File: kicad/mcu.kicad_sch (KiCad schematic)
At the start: 40 parts, among them J1 USB_C_Receptacle_USB2.0_16P, J2 2x5x1.27mm, U4 STM32F103CBT6, U5 USBLC6-2SC6, Y1 16MHz

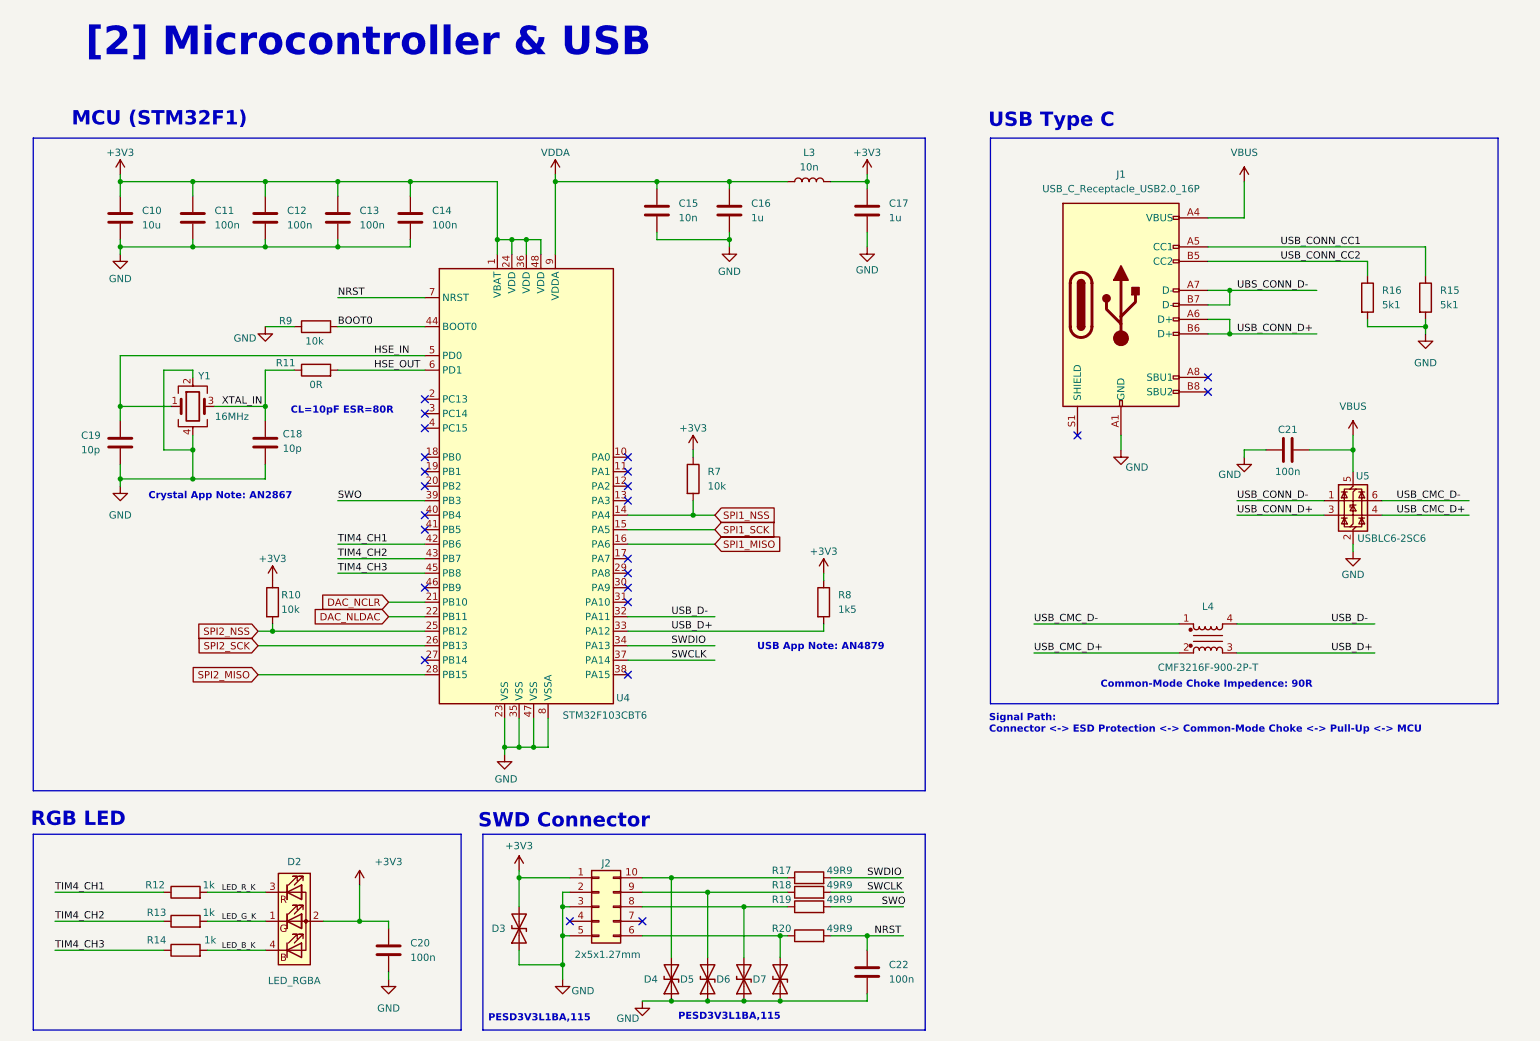
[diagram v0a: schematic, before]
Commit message: Updated parts numbering and notes
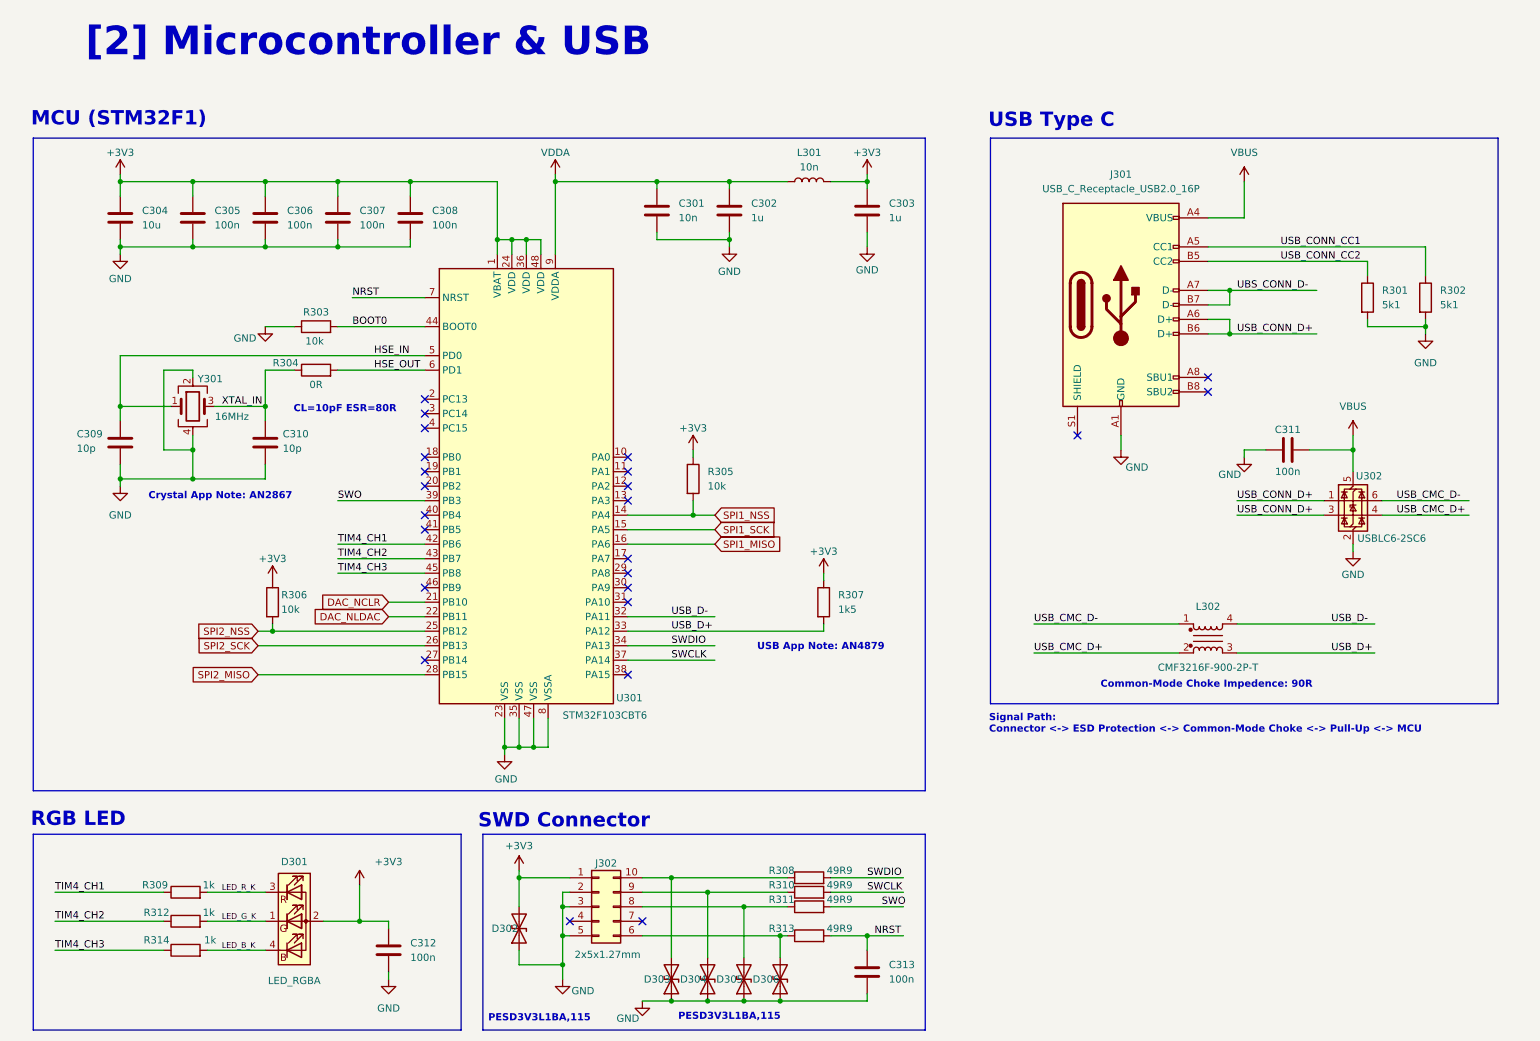
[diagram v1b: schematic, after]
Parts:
- renumbered C15 to C301, C16 to C302, C17 to C303, C10 to C304, C11 to C305, C12 to C306, C13 to C307, C14 to C308, C19 to C309, C18 to C310, C21 to C311, C20 to C312, C22 to C313, D2 to D301, D3 to D302, D4 to D303, D5 to D304, D6 to D305, D7 to D306, J1 to J301, J2 to J302, L3 to L301, L4 to L302, R16 to R301, R15 to R302, R9 to R303, R11 to R304, R7 to R305, R10 to R306, R8 to R307, R17 to R308, R12 to R309, R18 to R310, R19 to R311, R13 to R312, R20 to R313, R14 to R314, U4 to U301, U5 to U302, Y1 to Y301
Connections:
- net USB_CONN_D- is gone; now on net USB_CONN_D+: U302.1 (I/O1)

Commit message: Save Progress
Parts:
- C301, C302, C303, C304: footprint (none) -> Capacitor_SMD:C_0603_1608Metric
- C305, C306, C307, C308, C309, C310, C311, C312, C313: footprint (none) -> Capacitor_SMD:C_0402_1005Metric
- D301: footprint (none) -> LED_SMD:LED_Avago_PLCC4_3.2x2.8mm_CW
- D302, D303, D304, D305, D306: value ~ -> D_TVS; footprint (none) -> Diode_SMD:D_SOD-323
- J301: footprint (none) -> Connector_USB:USB_C_Receptacle_HRO_TYPE-C-31-M-12
- J302: footprint (none) -> Connector_PinHeader_1.27mm:PinHeader_2x05_P1.27mm_Vertical_SMD
- L301: footprint (none) -> Inductor_SMD:L_0402_1005Metric
- R301, R302, R303, R304, R305, R306, R307, R308, R309, R310, R311, R312, R313, R314: footprint (none) -> Resistor_SMD:R_0402_1005Metric
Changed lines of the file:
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@@
 			)
 		)
-		(property "Footprint" ""
+		(property "Footprint" "Connector_USB:USB_C_Receptacle_HRO_TYPE-C-31-M-12"
 			(at 212.09 67.31 0)
 			(effects
@@
 			)
 		)
-		(property "Footprint" ""
+		(property "Footprint" "Capacitor_SMD:C_0603_1608Metric"
 			(at 140.6652 54.61 0)
 			(effects
@@
 			)
 		)
-		(property "Footprint" ""
+		(property "Footprint" "Capacitor_SMD:C_0402_1005Metric"
 			(at 72.0852 55.88 0)
 			(effects
@@
 			)
 		)
-		(property "Footprint" ""
+		(property "Footprint" "Capacitor_SMD:C_0603_1608Metric"
 			(at 33.9852 55.88 0)
 			(effects
@@
 			)
 		)
-		(property "Footprint" ""
+		(property "Footprint" "Resistor_SMD:R_0402_1005Metric"
 			(at 259.842 66.04 90)
 			(effects
@@
 		(dnp no)
 		(property "Reference" "D303"
-			(at 124.714 185.42 90)
+			(at 123.444 179.324 90)
 			(effects
 				(font
@@
 			)
 		)
-		(property "Value" "~"
-			(at 132.08 186.69 90)
+		(property "Value" "D_TVS"
+			(at 123.444 181.356 90)
 			(effects
 				(font
@@
 			)
 		)
-		(property "Footprint" ""
+		(property "Footprint" "Diode_SMD:D_SOD-323"
 			(at 129.54 185.42 0)
 			(effects
@@
 			)
 		)
-		(property "Footprint" ""
+		(property "Footprint" "Resistor_SMD:R_0402_1005Metric"
 			(at 154.432 119.38 90)
 			(effects
@@
 			)
 		)
-		(property "Footprint" ""
+		(property "Footprint" "Resistor_SMD:R_0402_1005Metric"
 			(at 153.67 171.958 90)
 			(effects
@@
 			)
 		)
-		(property "Footprint" ""
+		(property "Footprint" "Capacitor_SMD:C_0402_1005Metric"
 			(at 164.7952 187.96 0)
 			(effects
@@
 			)
 		)
-		(property "Footprint" ""
+		(property "Footprint" "Resistor_SMD:R_0402_1005Metric"
 			(at 67.31 80.518 90)
 			(effects
@@
 			)
 		)
-		(property "Footprint" ""
+		(property "Footprint" "Resistor_SMD:R_0402_1005Metric"
 			(at 44.45 171.958 90)
 			(effects
@@
 			)
 		)
-		(property "Footprint" ""
+		(property "Footprint" "Capacitor_SMD:C_0402_1005Metric"
 			(at 84.7852 55.88 0)
 			(effects
@@
 			)
 		)
-		(property "Footprint" ""
+		(property "Footprint" "Resistor_SMD:R_0402_1005Metric"
 			(at 44.45 177.038 90)
 			(effects
@@
 		(dnp no)
 		(property "Reference" "D302"
-			(at 98.044 176.53 90)
+			(at 104.14 175.514 90)
 			(effects
 				(font
@@
 			)
 		)
-		(property "Value" "~"
-			(at 105.41 177.8 90)
+		(property "Value" "D_TVS"
+			(at 104.14 177.8 90)
 			(effects
 				(font
@@
 			)
 		)
-		(property "Footprint" ""
+		(property "Footprint" "Diode_SMD:D_SOD-323"
 			(at 102.87 176.53 0)
 			(effects
@@
 			)
 		)
-		(property "Footprint" ""
+		(property "Footprint" "Capacitor_SMD:C_0603_1608Metric"
 			(at 164.7952 54.61 0)
 			(effects
@@
 			)
 		)
-		(property "Footprint" ""
+		(property "Footprint" "Capacitor_SMD:C_0402_1005Metric"
 			(at 46.6852 55.88 0)
 			(effects
@@
 			)
 		)
-		(property "Footprint" ""
+		(property "Footprint" "Resistor_SMD:R_0402_1005Metric"
 			(at 131.572 97.79 90)
 			(effects
@@
 		(dnp no)
 		(property "Reference" "D304"
-			(at 131.064 185.42 90)
+			(at 130.048 179.324 90)
 			(effects
 				(font
@@
 			)
 		)
-		(property "Value" "~"
-			(at 138.43 186.69 90)
+		(property "Value" "D_TVS"
+			(at 130.048 181.356 90)
 			(effects
 				(font
@@
 			)
 		)
-		(property "Footprint" ""
+		(property "Footprint" "Diode_SMD:D_SOD-323"
 			(at 135.89 185.42 0)
 			(effects
@@
 			)
 		)
-		(property "Footprint" ""
+		(property "Footprint" "Inductor_SMD:L_0402_1005Metric"
 			(at 153.67 45.72 0)
 			(effects
@@
 			)
 		)
-		(property "Footprint" ""
+		(property "Footprint" "Resistor_SMD:R_0402_1005Metric"
 			(at 153.67 174.498 90)
 			(effects
@@
 			)
 		)
-		(property "Footprint" ""
+		(property "Footprint" "Capacitor_SMD:C_0402_1005Metric"
 			(at 59.3852 55.88 0)
 			(effects
@@
 			)
 		)
-		(property "Footprint" ""
+		(property "Footprint" "Resistor_SMD:R_0402_1005Metric"
 			(at 57.912 119.38 90)
 			(effects
@@
 			)
 		)
-		(property "Footprint" ""
+		(property "Footprint" "Capacitor_SMD:C_0402_1005Metric"
 			(at 59.3852 95.25 0)
 			(effects
@@
 			)
 		)
-		(property "Footprint" ""
+		(property "Footprint" "Resistor_SMD:R_0402_1005Metric"
 			(at 249.682 66.04 90)
 			(effects
@@
 			)
 		)
-		(property "Footprint" ""
+		(property "Footprint" "Resistor_SMD:R_0402_1005Metric"
 			(at 44.45 182.118 90)
 			(effects
@@
 		)
 		(property "Value" "2x5x1.27mm"
-			(at 118.364 181.102 0)
+			(at 116.84 180.594 0)
 			(effects
 				(font
@@
 			)
 		)
-		(property "Footprint" ""
+		(property "Footprint" "Connector_PinHeader_1.27mm:PinHeader_2x05_P1.27mm_Vertical_SMD"
 			(at 116.84 172.72 0)
 			(effects
@@
 			)
 		)
-		(property "Footprint" ""
+		(property "Footprint" "Capacitor_SMD:C_0402_1005Metric"
 			(at 33.9852 95.25 0)
 			(effects
@@
 			)
 		)
-		(property "Footprint" ""
+		(property "Footprint" "Capacitor_SMD:C_0402_1005Metric"
 			(at 241.3 91.7448 0)
 			(effects
@@
 			)
 		)
-		(property "Footprint" ""
+		(property "Footprint" "Capacitor_SMD:C_0402_1005Metric"
 			(at 80.9752 184.15 0)
 			(effects
@@
 		(dnp no)
 		(property "Reference" "D306"
-			(at 143.764 185.42 90)
+			(at 142.748 179.324 90)
 			(effects
 				(font
@@
 			)
 		)
-		(property "Value" "~"
-			(at 151.13 186.69 90)
+		(property "Value" "D_TVS"
+			(at 142.748 181.356 90)
 			(effects
 				(font
@@
 			)
 		)
-		(property "Footprint" ""
+		(property "Footprint" "Diode_SMD:D_SOD-323"
 			(at 148.59 185.42 0)
 			(effects
@@
 			)
 		)
-		(property "Footprint" ""
+		(property "Footprint" "LED_SMD:LED_Avago_PLCC4_3.2x2.8mm_CW"
 			(at 63.5 176.53 0)
 			(effects
@@
 			)
 		)
-		(property "Footprint" ""
+		(property "Footprint" "Resistor_SMD:R_0402_1005Metric"
 			(at 67.31 72.898 90)
 			(effects
@@
 			)
 		)
-		(property "Footprint" ""
+		(property "Footprint" "Resistor_SMD:R_0402_1005Metric"
 			(at 153.67 169.418 90)
 			(effects
@@
 		(dnp no)
 		(property "Reference" "D305"
-			(at 137.414 185.42 90)
+			(at 136.398 179.324 90)
 			(effects
 				(font
@@
 			)
 		)
-		(property "Value" "~"
-			(at 144.78 186.69 90)
+		(property "Value" "D_TVS"
+			(at 136.398 181.356 90)
 			(effects
 				(font
@@
 			)
 		)
-		(property "Footprint" ""
+		(property "Footprint" "Diode_SMD:D_SOD-323"
 			(at 142.24 185.42 0)
 			(effects
@@
 			)
 		)
-		(property "Footprint" ""
+		(property "Footprint" "Capacitor_SMD:C_0603_1608Metric"
 			(at 127.9652 54.61 0)
 			(effects
@@
 			)
 		)
-		(property "Footprint" ""
+		(property "Footprint" "Resistor_SMD:R_0402_1005Metric"
 			(at 153.67 179.578 90)
 			(effects
